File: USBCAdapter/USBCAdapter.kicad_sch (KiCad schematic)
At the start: 21 parts, among them J1 USB_C_Receptacle_USB2.0_16P, J2 Conn_01x02, J4 Conn_01x04_MountingPin, U1 TP4057, U2 TP4057

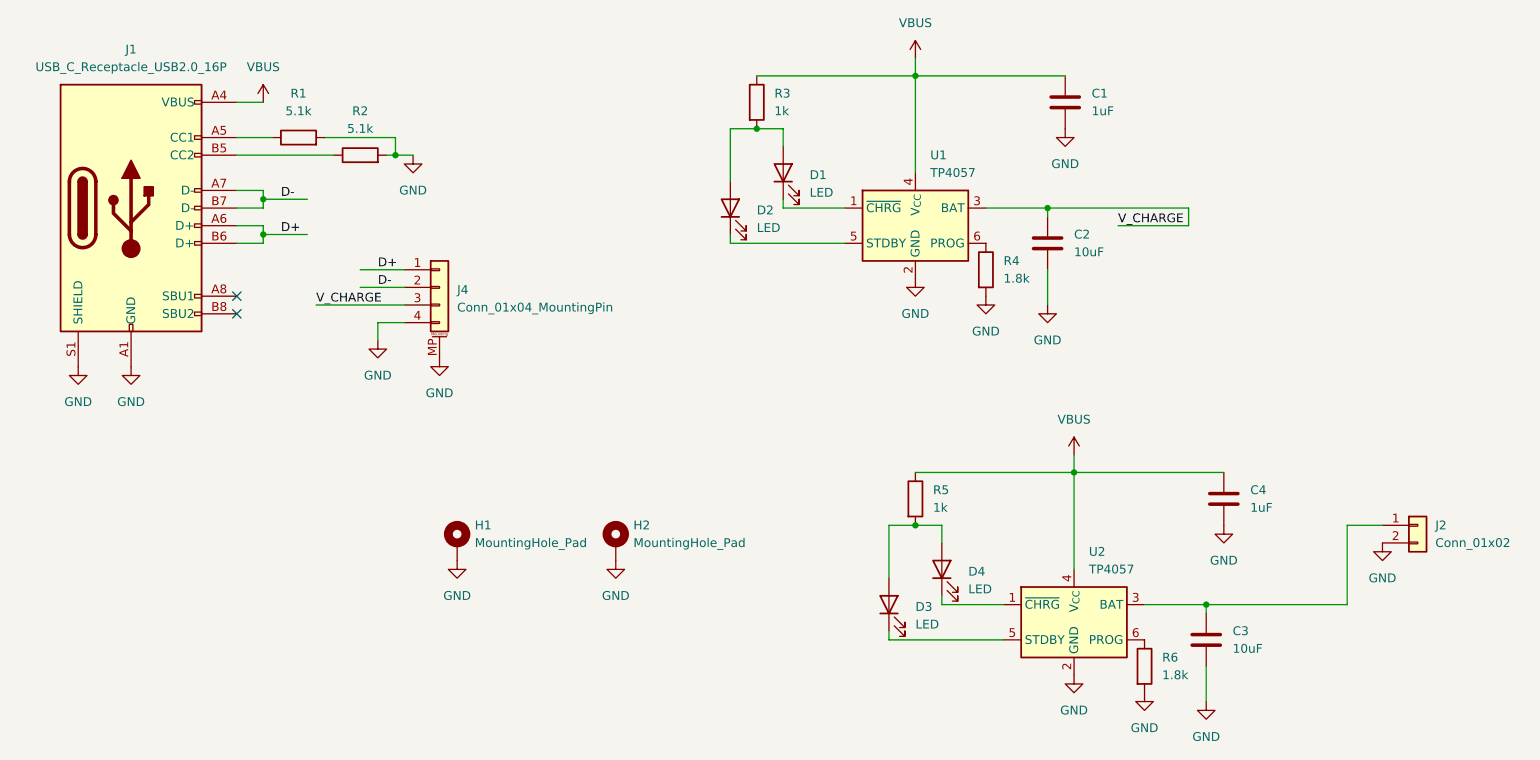
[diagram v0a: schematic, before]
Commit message: switched back to onboard charger and the most boring adapter board ever
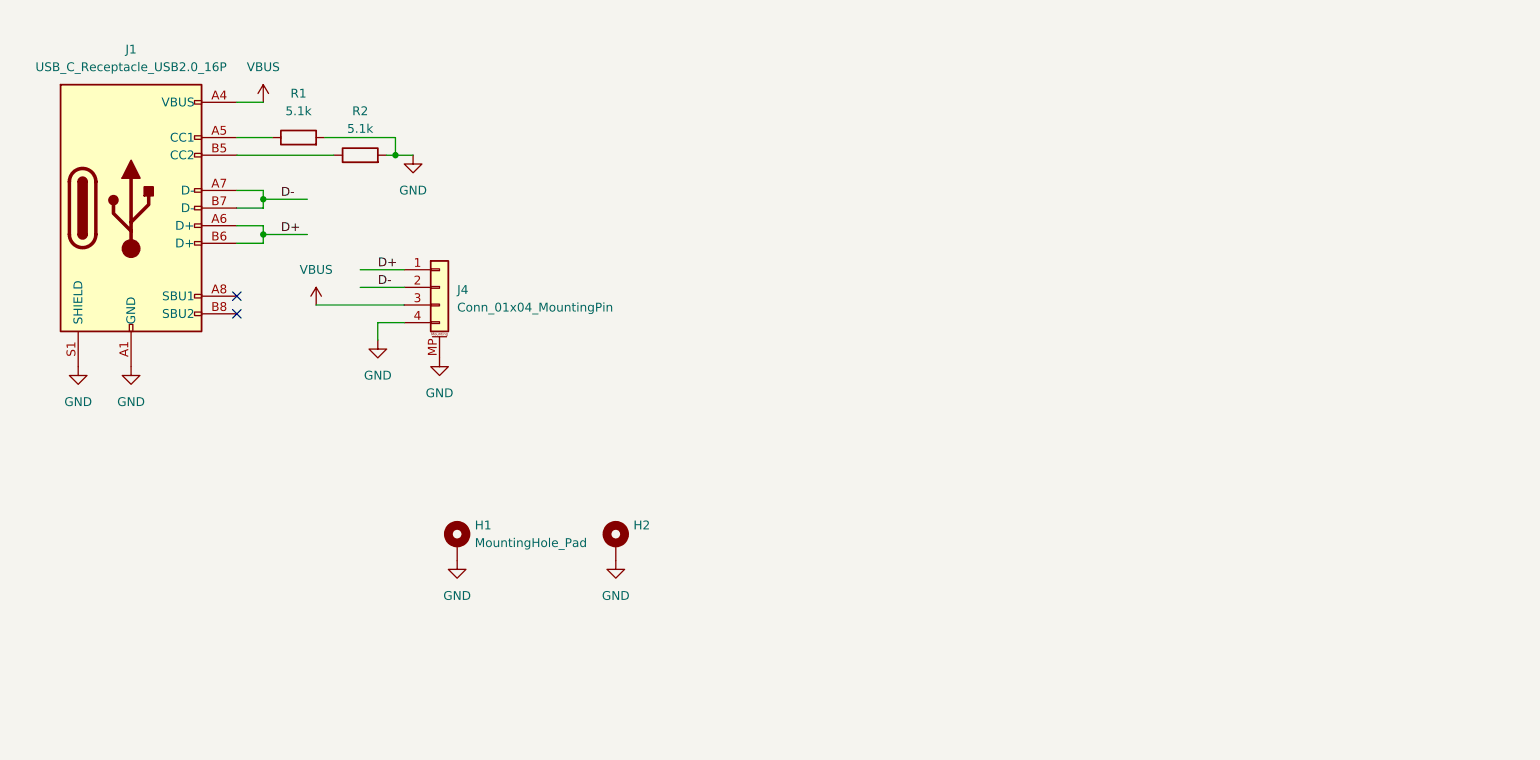
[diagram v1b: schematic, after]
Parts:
- removed C1, C4: 1uF, Capacitor_SMD:C_0603_1608Metric, symbol Device:C
- removed C2, C3: 10uF, Capacitor_SMD:C_0603_1608Metric, symbol Device:C
- removed D1, D2, D3, D4: LED, LED_SMD:LED_0603_1608Metric, symbol Device:LED
- removed J2: Conn_01x02, Connector_JST:JST_PH_S2B-PH-K_1x02_P2.00mm_Horizontal, symbol Connector_Generic:Conn_01x02
- removed R3, R5: 1k, Resistor_SMD:R_0603_1608Metric, symbol Device:R
- removed R4, R6: 1.8k, Resistor_SMD:R_0603_1608Metric, symbol Device:R
- removed U1, U2: TP4057, Package_TO_SOT_SMD:TSOT-23-6, symbol Battery_Management:TP4057
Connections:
- net V_CHARGE is gone; now on net VBUS: J4.3 (Pin_3)
